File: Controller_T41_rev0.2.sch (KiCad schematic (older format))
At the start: 54 parts, among them J1 8P8C_x4, J2 8P8C_x4, J3 Screw_Terminal_01x02, J4 RJ45_LED, U1 Teensy4.1, U2 AMS1117-5.0, U3 74HC245, U4 74HC245, U5 74HC245, U6 74HC245

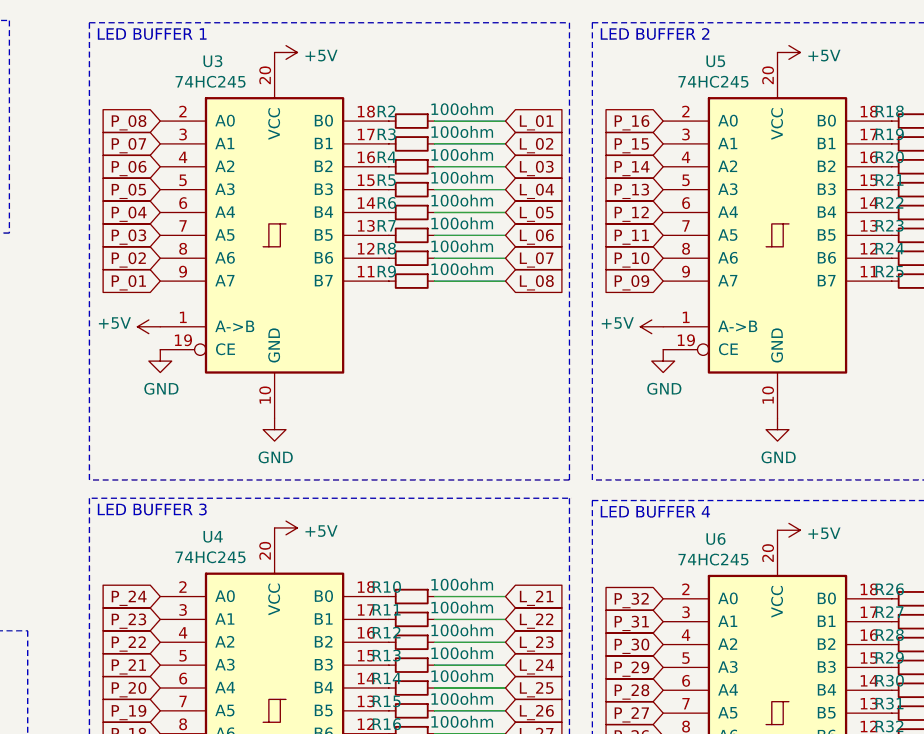
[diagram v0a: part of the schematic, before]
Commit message: Changed buffer to 74HCT245 from 74HC245
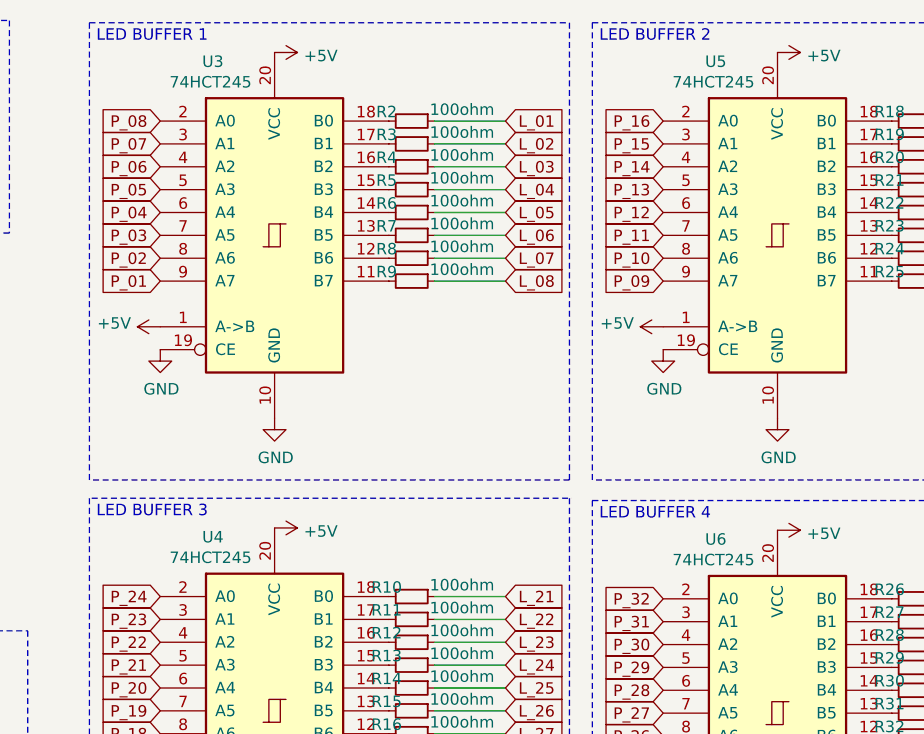
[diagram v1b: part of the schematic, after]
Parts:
- U3, U4, U5, U6: value 74HC245 -> 74HCT245
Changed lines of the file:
@@
 P 4860 1530
 F 0 "U3" H 4590 2290 50  0000 C CNN
-F 1 "74HC245" H 4580 2200 50  0000 C CNN
+F 1 "74HCT245" H 4580 2200 50  0000 C CNN
 F 2 "Package_SO:SOIC-20W_7.5x12.8mm_P1.27mm" H 4860 1530 50  0001 C CNN
 F 3 "http://www.ti.com/lit/gpn/sn74HC245" H 4860 1530 50  0001 C CNN
@@
 P 4860 3610
 F 0 "U4" H 4590 4370 50  0000 C CNN
-F 1 "74HC245" H 4580 4280 50  0000 C CNN
+F 1 "74HCT245" H 4580 4280 50  0000 C CNN
 F 2 "Package_SO:SOIC-20W_7.5x12.8mm_P1.27mm" H 4860 3610 50  0001 C CNN
 F 3 "http://www.ti.com/lit/gpn/sn74HC245" H 4860 3610 50  0001 C CNN
@@
 P 7060 3620
 F 0 "U6" H 6790 4380 50  0000 C CNN
-F 1 "74HC245" H 6780 4290 50  0000 C CNN
+F 1 "74HCT245" H 6780 4290 50  0000 C CNN
 F 2 "Package_SO:SOIC-20W_7.5x12.8mm_P1.27mm" H 7060 3620 50  0001 C CNN
 F 3 "http://www.ti.com/lit/gpn/sn74HC245" H 7060 3620 50  0001 C CNN
@@
 P 7060 1530
 F 0 "U5" H 6790 2290 50  0000 C CNN
-F 1 "74HC245" H 6780 2200 50  0000 C CNN
+F 1 "74HCT245" H 6780 2200 50  0000 C CNN
 F 2 "Package_SO:SOIC-20W_7.5x12.8mm_P1.27mm" H 7060 1530 50  0001 C CNN
 F 3 "http://www.ti.com/lit/gpn/sn74HC245" H 7060 1530 50  0001 C CNN

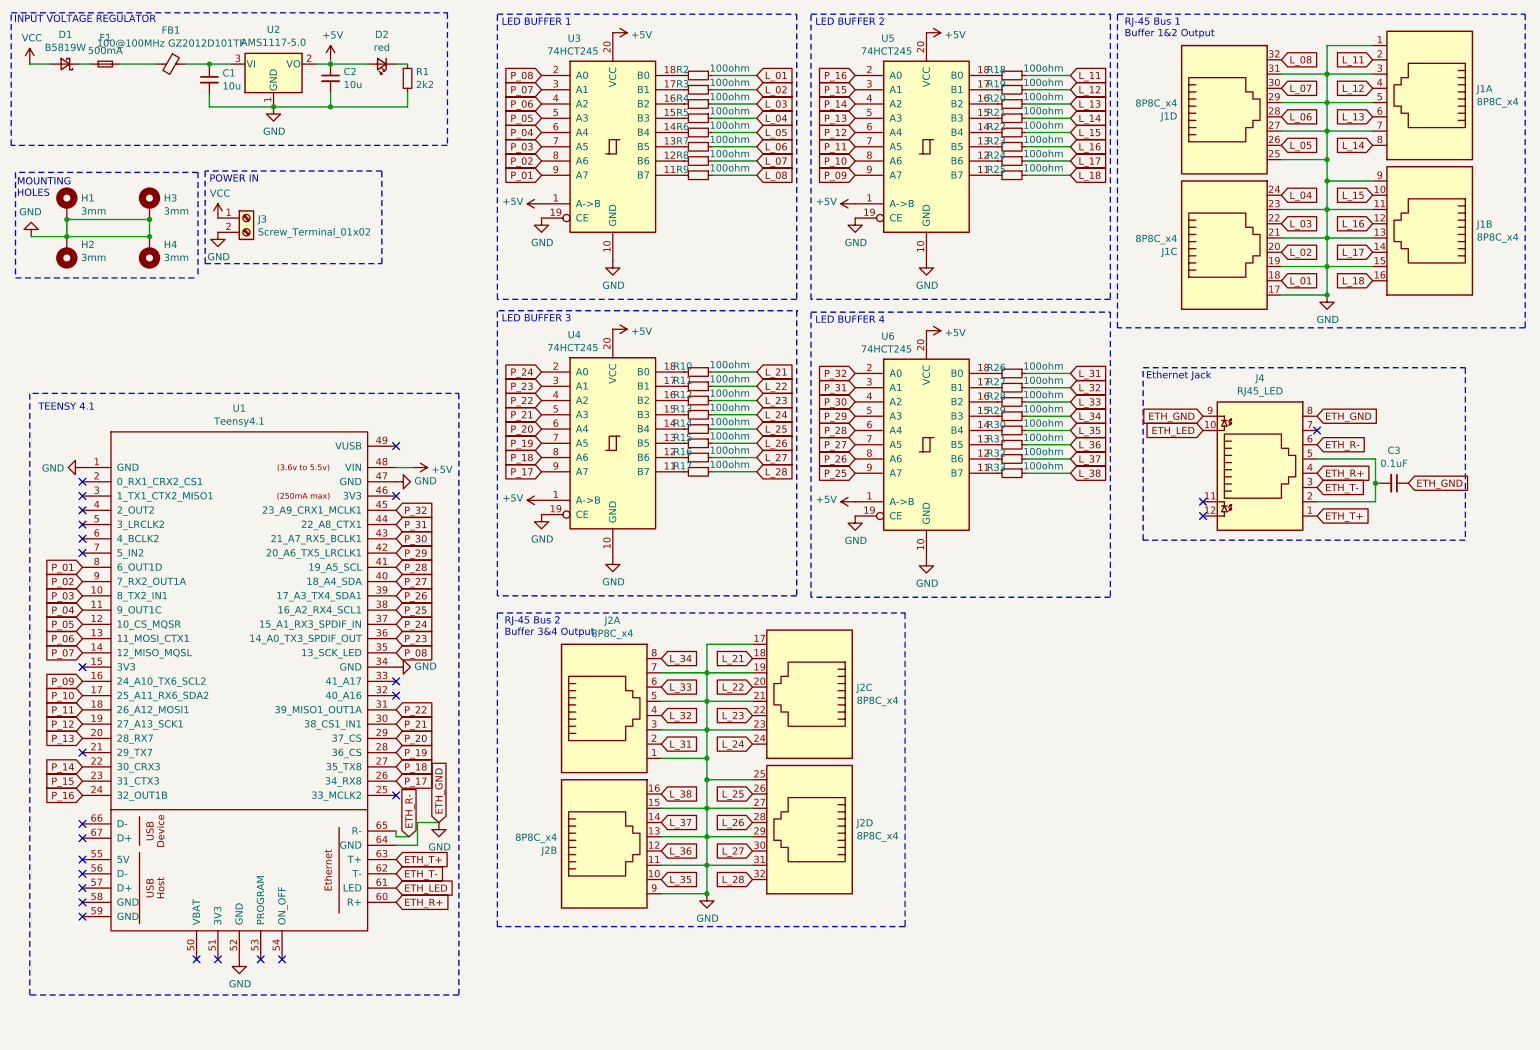
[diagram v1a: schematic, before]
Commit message: Updated schematic layout and parts. Minor updates to footprint.
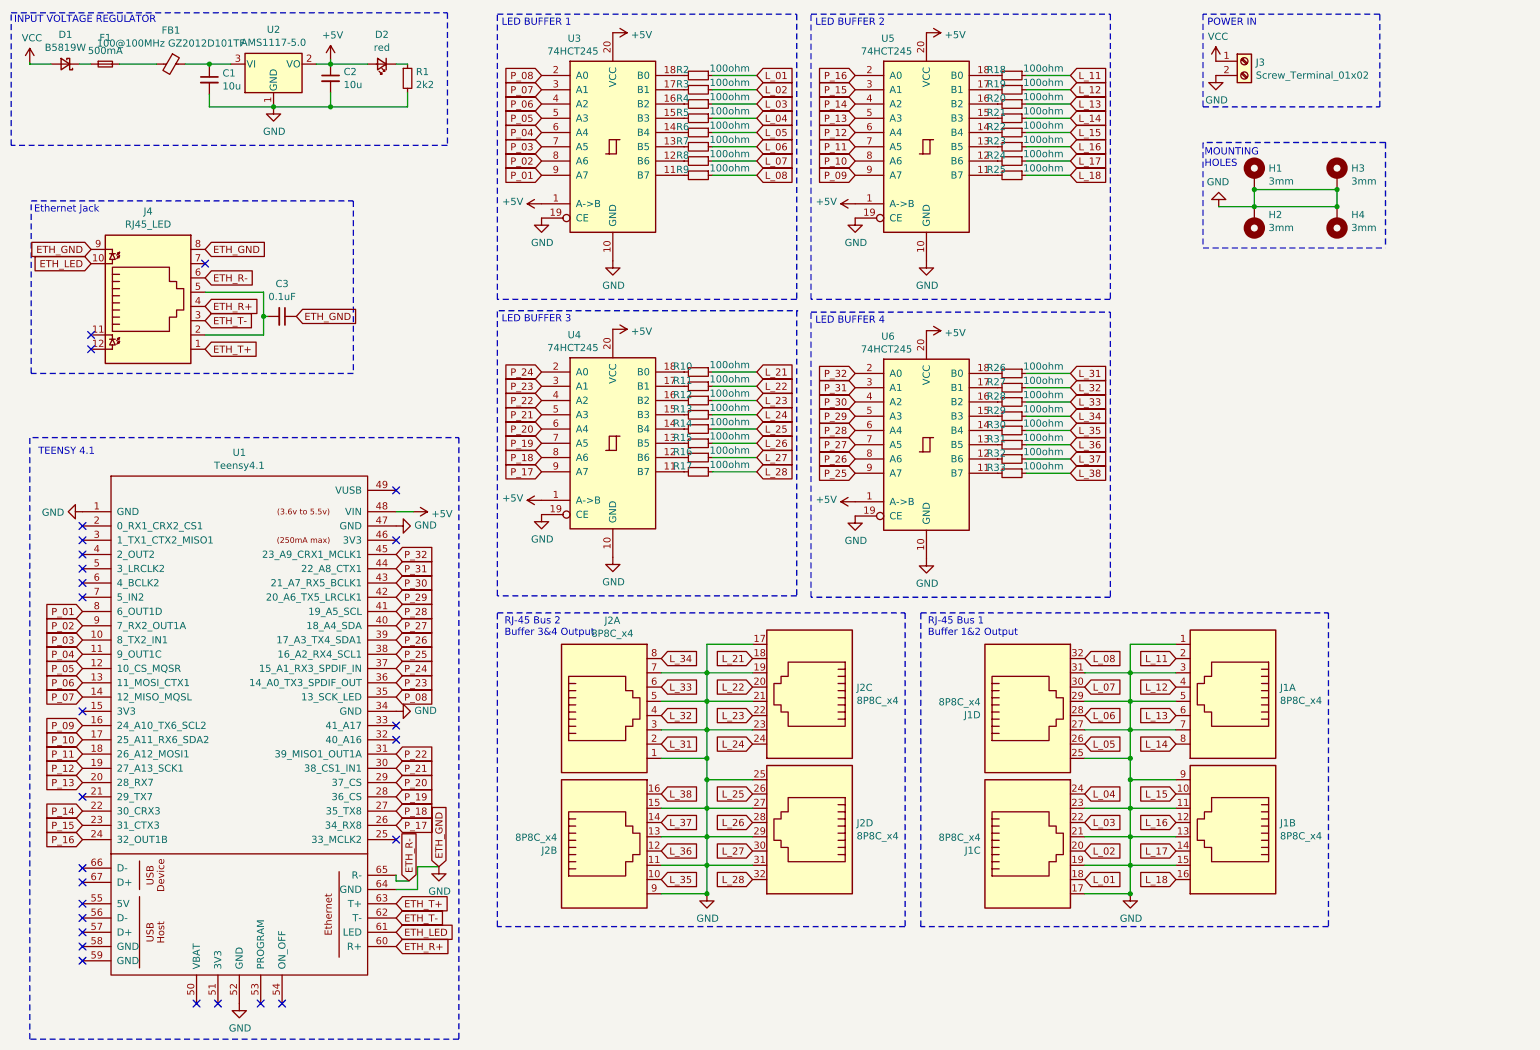
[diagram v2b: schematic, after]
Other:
- moved on the sheet: C3, H1, H2, H3, H4, J1A, J1B, J1C, J1D, J3, J4, U1

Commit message: Updated some parts on LCSC and some smt components
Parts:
- C1, C2: LCSC (none) -> C13585
- C3: LCSC (none) -> C49678
- D1: LCSC (none) -> C8598
- D2: footprint LED_SMD:LED_0805_2012Metric -> LED_SMD:LED_0603_1608Metric; LCSC (none) -> C2286
- FB1: LCSC (none) -> C1015
- R1: LCSC (none) -> C17520
- R10, R11, R12, R13, R14, R15, R16, R17, R18, R19, R2, R20, R21, R22, R23, R24, R25, R26, R27, R28, R29, R3, R30, R31, R32, R33, R4, R5, R6, R7, R8, R9: LCSC (none) -> C17901
- U2: LCSC (none) -> C6187
- U3, U4, U5, U6: LCSC (none) -> C110789
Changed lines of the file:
@@
 F 2 "Package_TO_SOT_SMD:SOT-223-3_TabPin2" H 2480 1150 50  0001 C CNN
 F 3 "http://www.advanced-monolithic.com/pdf/ds1117.pdf" H 2580 700 50  0001 C CNN
+F 4 "C6187" H 2480 950 50  0001 C CNN "LCSC"
 	1    2480 950
 	1    0    0    -1
@@
 F 1 "10u" H 2122 1015 50  0000 L CNN
 F 2 "Capacitor_SMD:C_1206_3216Metric" H 2030 1060 50  0001 C CNN
-F 3 "~" H 2030 1060 50  0001 C CNN
+F 3 "https://datasheet.lcsc.com/szlcsc/Samsung-Electro-Mechanics-CL31A106KBHNNNE_C13585.pdf" H 2030 1060 50  0001 C CNN
+F 4 "C13585" H 2030 1060 50  0001 C CNN "LCSC"
 	1    2030 1060
 	1    0    0    -1
@@
 F 1 "10u" H 2972 1005 50  0000 L CNN
 F 2 "Capacitor_SMD:C_1206_3216Metric" H 2880 1050 50  0001 C CNN
-F 3 "~" H 2880 1050 50  0001 C CNN
+F 3 "https://datasheet.lcsc.com/szlcsc/Samsung-Electro-Mechanics-CL31A106KBHNNNE_C13585.pdf" H 2880 1050 50  0001 C CNN
+F 4 "C13585" H 2880 1050 50  0001 C CNN "LCSC"
 	1    2880 1050
 	1    0    0    -1
@@
 F 2 "Inductor_SMD:L_0805_2012Metric" V 1690 950 50  0001 C CNN
 F 3 "~" H 1760 950 50  0001 C CNN
+F 4 " C1015" V 1760 950 50  0001 C CNN "LCSC"
 	1    1760 950
 	0    1    1    0
@@
 F 2 "Fuse:Fuse_0603_1608Metric_Pad1.05x0.95mm_HandSolder" H 1300 950 50  0001 C CNN
 F 3 "~" H 1300 950 50  0001 C CNN
+F 4 "" H 1300 950 50  0001 C CNN "LCSC"
 	1    1300 950
 	1    0    0    -1
@@
 F 2 "Diode_SMD:D_SOD-123" V 1020 950 50  0001 C CNN
 F 3 "~" V 1020 950 50  0001 C CNN
+F 4 "C8598" H 1020 950 50  0001 C CNN "LCSC"
 	1    1020 950
 	-1   0    0    1
@@
 F 0 "D2" H 3240 743 50  0000 C CNN
 F 1 "red" H 3240 834 50  0000 C CNN
-F 2 "LED_SMD:LED_0805_2012Metric" V 3240 950 50  0001 C CNN
+F 2 "LED_SMD:LED_0603_1608Metric" V 3240 950 50  0001 C CNN
 F 3 "~" V 3240 950 50  0001 C CNN
+F 4 "C2286" H 3240 950 50  0001 C CNN "LCSC"
 	1    3240 950
 	-1   0    0    1
@@
 F 2 "Resistor_SMD:R_0805_2012Metric" H 3420 1050 50  0001 C CNN
 F 3 "~" H 3420 1050 50  0001 C CNN
+F 4 "C17520" H 3420 1050 50  0001 C CNN "LCSC"
 	1    3420 1050
 	1    0    0    -1
@@
 F 2 "Package_SO:SOIC-20W_7.5x12.8mm_P1.27mm" H 4860 1530 50  0001 C CNN
 F 3 "http://www.ti.com/lit/gpn/sn74HC245" H 4860 1530 50  0001 C CNN
+F 4 "C110789" H 4860 1530 50  0001 C CNN "LCSC"
 	1    4860 1530
 	1    0    0    -1
@@
 F 2 "Resistor_SMD:R_1206_3216Metric" H 5460 1030 50  0001 C CNN
 F 3 "~" H 5460 1030 50  0001 C CNN
+F 4 "C17901" V 5460 1030 50  0001 C CNN "LCSC"
 	1    5460 1030
 	0    1    1    0
@@
 F 2 "Resistor_SMD:R_1206_3216Metric" H 5460 1130 50  0001 C CNN
 F 3 "~" H 5460 1130 50  0001 C CNN
+F 4 "C17901" V 5460 1130 50  0001 C CNN "LCSC"
 	1    5460 1130
 	0    1    1    0
@@
 F 2 "Resistor_SMD:R_1206_3216Metric" H 5460 1230 50  0001 C CNN
 F 3 "~" H 5460 1230 50  0001 C CNN
+F 4 "C17901" V 5460 1230 50  0001 C CNN "LCSC"
 	1    5460 1230
 	0    1    1    0
@@
 F 2 "Resistor_SMD:R_1206_3216Metric" H 5460 1330 50  0001 C CNN
 F 3 "~" H 5460 1330 50  0001 C CNN
+F 4 "C17901" V 5460 1330 50  0001 C CNN "LCSC"
 	1    5460 1330
 	0    1    1    0
@@
 F 2 "Resistor_SMD:R_1206_3216Metric" H 5460 1430 50  0001 C CNN
 F 3 "~" H 5460 1430 50  0001 C CNN
+F 4 "C17901" V 5460 1430 50  0001 C CNN "LCSC"
 	1    5460 1430
 	0    1    1    0
@@
 F 2 "Resistor_SMD:R_1206_3216Metric" H 5460 1530 50  0001 C CNN
 F 3 "~" H 5460 1530 50  0001 C CNN
+F 4 "C17901" V 5460 1530 50  0001 C CNN "LCSC"
 	1    5460 1530
 	0    1    1    0
@@
 F 2 "Resistor_SMD:R_1206_3216Metric" H 5460 1630 50  0001 C CNN
 F 3 "~" H 5460 1630 50  0001 C CNN
+F 4 "C17901" V 5460 1630 50  0001 C CNN "LCSC"
 	1    5460 1630
 	0    1    1    0
@@
 F 2 "Resistor_SMD:R_1206_3216Metric" H 5460 1730 50  0001 C CNN
 F 3 "~" H 5460 1730 50  0001 C CNN
+F 4 "C17901" V 5460 1730 50  0001 C CNN "LCSC"
 	1    5460 1730
 	0    1    1    0
@@
 F 2 "Package_SO:SOIC-20W_7.5x12.8mm_P1.27mm" H 4860 3610 50  0001 C CNN
 F 3 "http://www.ti.com/lit/gpn/sn74HC245" H 4860 3610 50  0001 C CNN
+F 4 "C110789" H 4860 3610 50  0001 C CNN "LCSC"
 	1    4860 3610
 	1    0    0    -1
@@
 F 2 "Resistor_SMD:R_1206_3216Metric" H 5460 3110 50  0001 C CNN
 F 3 "~" H 5460 3110 50  0001 C CNN
+F 4 "C17901" V 5460 3110 50  0001 C CNN "LCSC"
 	1    5460 3110
 	0    1    1    0
@@
 F 2 "Resistor_SMD:R_1206_3216Metric" H 5460 3210 50  0001 C CNN
 F 3 "~" H 5460 3210 50  0001 C CNN
+F 4 "C17901" V 5460 3210 50  0001 C CNN "LCSC"
 	1    5460 3210
 	0    1    1    0
@@
 F 2 "Resistor_SMD:R_1206_3216Metric" H 5460 3310 50  0001 C CNN
 F 3 "~" H 5460 3310 50  0001 C CNN
+F 4 "C17901" V 5460 3310 50  0001 C CNN "LCSC"
 	1    5460 3310
 	0    1    1    0
@@
 F 2 "Resistor_SMD:R_1206_3216Metric" H 5460 3410 50  0001 C CNN
 F 3 "~" H 5460 3410 50  0001 C CNN
+F 4 "C17901" V 5460 3410 50  0001 C CNN "LCSC"
 	1    5460 3410
 	0    1    1    0
@@
 F 2 "Resistor_SMD:R_1206_3216Metric" H 5460 3510 50  0001 C CNN
 F 3 "~" H 5460 3510 50  0001 C CNN
+F 4 "C17901" V 5460 3510 50  0001 C CNN "LCSC"
 	1    5460 3510
 	0    1    1    0
@@
 F 2 "Resistor_SMD:R_1206_3216Metric" H 5460 3610 50  0001 C CNN
 F 3 "~" H 5460 3610 50  0001 C CNN
+F 4 "C17901" V 5460 3610 50  0001 C CNN "LCSC"
 	1    5460 3610
 	0    1    1    0
@@
 F 2 "Resistor_SMD:R_1206_3216Metric" H 5460 3710 50  0001 C CNN
 F 3 "~" H 5460 3710 50  0001 C CNN
+F 4 "C17901" V 5460 3710 50  0001 C CNN "LCSC"
 	1    5460 3710
 	0    1    1    0
@@
 F 2 "Resistor_SMD:R_1206_3216Metric" H 5460 3810 50  0001 C CNN
 F 3 "~" H 5460 3810 50  0001 C CNN
+F 4 "C17901" V 5460 3810 50  0001 C CNN "LCSC"
 	1    5460 3810
 	0    1    1    0
@@
 F 2 "Resistor_SMD:R_1206_3216Metric" H 7660 3820 50  0001 C CNN
 F 3 "~" H 7660 3820 50  0001 C CNN
+F 4 "C17901" V 7660 3820 50  0001 C CNN "LCSC"
 	1    7660 3820
 	0    1    1    0
@@
 F 2 "Resistor_SMD:R_1206_3216Metric" H 7660 3720 50  0001 C CNN
 F 3 "~" H 7660 3720 50  0001 C CNN
+F 4 "C17901" V 7660 3720 50  0001 C CNN "LCSC"
 	1    7660 3720
 	0    1    1    0
@@
 F 2 "Resistor_SMD:R_1206_3216Metric" H 7660 3620 50  0001 C CNN
 F 3 "~" H 7660 3620 50  0001 C CNN
+F 4 "C17901" V 7660 3620 50  0001 C CNN "LCSC"
 	1    7660 3620
 	0    1    1    0
@@
 F 2 "Resistor_SMD:R_1206_3216Metric" H 7660 3520 50  0001 C CNN
 F 3 "~" H 7660 3520 50  0001 C CNN
+F 4 "C17901" V 7660 3520 50  0001 C CNN "LCSC"
 	1    7660 3520
 	0    1    1    0
@@
 F 2 "Resistor_SMD:R_1206_3216Metric" H 7660 3420 50  0001 C CNN
 F 3 "~" H 7660 3420 50  0001 C CNN
+F 4 "C17901" V 7660 3420 50  0001 C CNN "LCSC"
 	1    7660 3420
 	0    1    1    0
@@
 F 2 "Resistor_SMD:R_1206_3216Metric" H 7660 3320 50  0001 C CNN
 F 3 "~" H 7660 3320 50  0001 C CNN
+F 4 "C17901" V 7660 3320 50  0001 C CNN "LCSC"
 	1    7660 3320
 	0    1    1    0
@@
 F 2 "Resistor_SMD:R_1206_3216Metric" H 7660 3220 50  0001 C CNN
 F 3 "~" H 7660 3220 50  0001 C CNN
+F 4 "C17901" V 7660 3220 50  0001 C CNN "LCSC"
 	1    7660 3220
 	0    1    1    0
@@
 F 2 "Resistor_SMD:R_1206_3216Metric" H 7660 3120 50  0001 C CNN
 F 3 "~" H 7660 3120 50  0001 C CNN
+F 4 "C17901" V 7660 3120 50  0001 C CNN "LCSC"
 	1    7660 3120
 	0    1    1    0
@@
 F 2 "Package_SO:SOIC-20W_7.5x12.8mm_P1.27mm" H 7060 3620 50  0001 C CNN
 F 3 "http://www.ti.com/lit/gpn/sn74HC245" H 7060 3620 50  0001 C CNN
+F 4 "C110789" H 7060 3620 50  0001 C CNN "LCSC"
 	1    7060 3620
 	1    0    0    -1
@@
 F 2 "Resistor_SMD:R_1206_3216Metric" H 7660 1730 50  0001 C CNN
 F 3 "~" H 7660 1730 50  0001 C CNN
+F 4 "C17901" V 7660 1730 50  0001 C CNN "LCSC"
 	1    7660 1730
 	0    1    1    0
@@
 F 2 "Resistor_SMD:R_1206_3216Metric" H 7660 1630 50  0001 C CNN
 F 3 "~" H 7660 1630 50  0001 C CNN
+F 4 "C17901" V 7660 1630 50  0001 C CNN "LCSC"
 	1    7660 1630
 	0    1    1    0
@@
 F 2 "Resistor_SMD:R_1206_3216Metric" H 7660 1530 50  0001 C CNN
 F 3 "~" H 7660 1530 50  0001 C CNN
+F 4 "C17901" V 7660 1530 50  0001 C CNN "LCSC"
 	1    7660 1530
 	0    1    1    0
@@
 F 2 "Resistor_SMD:R_1206_3216Metric" H 7660 1430 50  0001 C CNN
 F 3 "~" H 7660 1430 50  0001 C CNN
+F 4 "C17901" V 7660 1430 50  0001 C CNN "LCSC"
 	1    7660 1430
 	0    1    1    0
@@
 F 2 "Resistor_SMD:R_1206_3216Metric" H 7660 1330 50  0001 C CNN
 F 3 "~" H 7660 1330 50  0001 C CNN
+F 4 "C17901" V 7660 1330 50  0001 C CNN "LCSC"
 	1    7660 1330
 	0    1    1    0
@@
 F 2 "Resistor_SMD:R_1206_3216Metric" H 7660 1230 50  0001 C CNN
 F 3 "~" H 7660 1230 50  0001 C CNN
+F 4 "C17901" V 7660 1230 50  0001 C CNN "LCSC"
 	1    7660 1230
 	0    1    1    0
@@
 F 2 "Resistor_SMD:R_1206_3216Metric" H 7660 1130 50  0001 C CNN
 F 3 "~" H 7660 1130 50  0001 C CNN
+F 4 "C17901" V 7660 1130 50  0001 C CNN "LCSC"
 	1    7660 1130
 	0    1    1    0
@@
 F 2 "Resistor_SMD:R_1206_3216Metric" H 7660 1030 50  0001 C CNN
 F 3 "~" H 7660 1030 50  0001 C CNN
+F 4 "C17901" V 7660 1030 50  0001 C CNN "LCSC"
 	1    7660 1030
 	0    1    1    0
@@
 F 2 "Package_SO:SOIC-20W_7.5x12.8mm_P1.27mm" H 7060 1530 50  0001 C CNN
 F 3 "http://www.ti.com/lit/gpn/sn74HC245" H 7060 1530 50  0001 C CNN
+F 4 "C110789" H 7060 1530 50  0001 C CNN "LCSC"
 	1    7060 1530
 	1    0    0    -1
@@
 F 2 "Capacitor_SMD:C_0805_2012Metric" H 2540 2720 50  0001 C CNN
 F 3 "~" H 2540 2720 50  0001 C CNN
+F 4 "C49678" V 2540 2720 50  0001 C CNN "LCSC"
 	1    2540 2720
 	0    1    1    0

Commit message: Upgraded to Kicad 5.1.9
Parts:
- J1, J2: symbol Connector:8P8C_x4 -> Controller_T41_rev0.2-rescue:8P8C_x4-Connector
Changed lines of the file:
@@
 L_01
 $Comp
-L Connector:8P8C_x4 J1
+L Controller_T41_rev0.2-rescue:8P8C_x4-Connector J1
 U 3 1 5FBD3466
 P 7770 6920
@@
 $EndComp
 $Comp
-L Connector:8P8C_x4 J1
+L Controller_T41_rev0.2-rescue:8P8C_x4-Connector J1
 U 2 1 5FBCBC15
 P 9210 5820
@@
 $EndComp
 $Comp
-L Connector:8P8C_x4 J1
+L Controller_T41_rev0.2-rescue:8P8C_x4-Connector J1
 U 1 1 5FBAD18C
 P 9210 4870
@@
 $EndComp
 $Comp
-L Connector:8P8C_x4 J1
+L Controller_T41_rev0.2-rescue:8P8C_x4-Connector J1
 U 4 1 5FBDBC48
 P 7770 5970
@@
 L_21
 $Comp
-L Connector:8P8C_x4 J2
+L Controller_T41_rev0.2-rescue:8P8C_x4-Connector J2
 U 2 1 5FE1C52F
 P 4800 6920
@@
 $EndComp
 $Comp
-L Connector:8P8C_x4 J2
+L Controller_T41_rev0.2-rescue:8P8C_x4-Connector J2
 U 4 1 5FE1C535
 P 6240 5820
@@
 $EndComp
 $Comp
-L Connector:8P8C_x4 J2
+L Controller_T41_rev0.2-rescue:8P8C_x4-Connector J2
 U 3 1 5FE1C53B
 P 6240 4870
@@
 $EndComp
 $Comp
-L Connector:8P8C_x4 J2
+L Controller_T41_rev0.2-rescue:8P8C_x4-Connector J2
 U 1 1 5FE1C541
 P 4800 5970
